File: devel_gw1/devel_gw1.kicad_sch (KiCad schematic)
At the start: 179 parts, among them Q1 2N7002, Q10 2N7002, Q11 2N7002, Q12 2N7002, Q13 2N7002, Q14 2N7002, Q15 2N7002, Q16 2N7002, Q17 2N7002, Q18 2N7002, Q19 2N7002, Q2 2N7002, Q20 2N7002, Q21 2N7002, Q22 2N7002, Q23 2N7002, Q24 2N7002, Q25 2N7002, Q26 2N7002, Q27 2N7002, Q28 2N7002, Q29 2N7002, Q3 2N7002, Q30 2N7002, Q31 2N7002, Q32 2N7002, Q33 2N7002, Q34 2N7002, Q35 2N7002, Q36 2N7002, Q37 2N7002, Q38 2N7002, Q39 2N7002, Q4 2N7002, Q41 2N7002, Q5 2N7002, Q6 2N7002, Q7 2N7002, Q8 2N7002, Q9 2N7002, U1 GW1N-LV9QN88C6_I5_, U2 LM3480-3.3, U3 AP2202K-ADJ, U4 ESP-PSRAM32, U5 AT25SF081-XMHF-X, U6 AP62150Z6, X1 ASE-xxxMHz

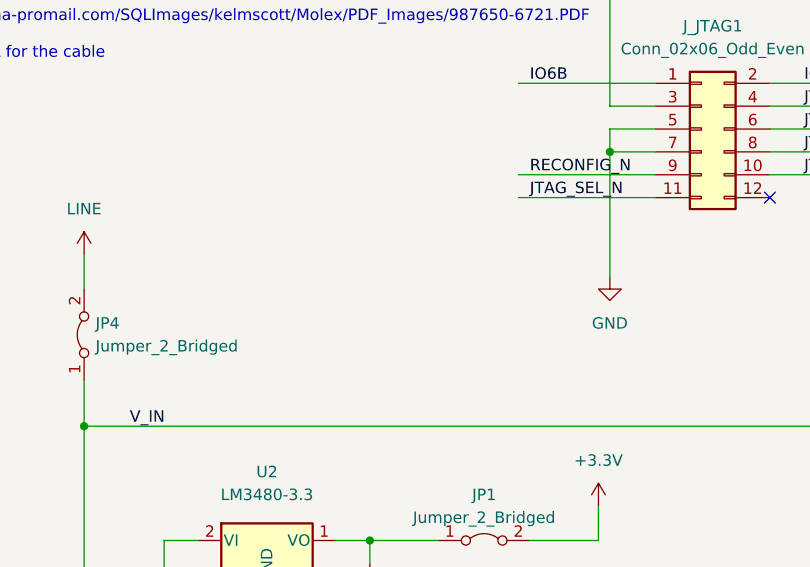
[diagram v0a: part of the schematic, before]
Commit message: Added power input connector
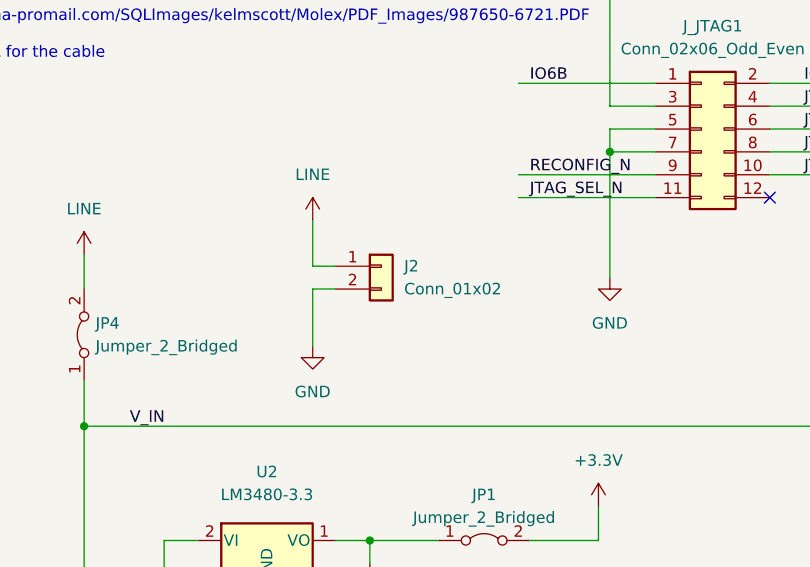
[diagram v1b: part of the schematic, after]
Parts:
- added J2: Conn_01x02, Connector_PinHeader_2.54mm:PinHeader_1x02_P2.54mm_Vertical, symbol Connector_Generic:Conn_01x02
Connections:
- net GND: now also J2.2 (Pin_2)
- net LINE: now also J2.1 (Pin_1)
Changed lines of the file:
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@@
     (stroke (width 0) (type default))
   )
+  (wire (pts (xy 157.48 220.98) (xy 157.48 226.06))
+    (stroke (width 0) (type default))
+  )
   (wire (pts (xy 228.6 71.12) (xy 228.6 73.66))
     (stroke (width 0) (type default))
@@
     (stroke (width 0) (type default))
   )
+  (wire (pts (xy 160.02 228.6) (xy 157.48 228.6))
+    (stroke (width 0) (type default))
+  )
   (wire (pts (xy 222.25 265.43) (xy 219.71 265.43))
     (stroke (width 0) (type default))
@@
     (stroke (width 0) (type default))
   )
+  (wire (pts (xy 160.02 226.06) (xy 157.48 226.06))
+    (stroke (width 0) (type default))
+  )
   (wire (pts (xy 107.95 154.94) (xy 133.35 154.94))
     (stroke (width 0) (type default))
@@
     (stroke (width 0) (type default))
   )
+  (wire (pts (xy 157.48 228.6) (xy 157.48 234.95))
+    (stroke (width 0) (type default))
+  )
   (wire (pts (xy 107.95 157.48) (xy 133.35 157.48))
     (stroke (width 0) (type default))
@@
     )
   )
+  (symbol (lib_id "Connector_Generic:Conn_01x02") (at 165.1 226.06 0) (unit 1)
+    (in_bom yes) (on_board yes) (dnp no) (fields_autoplaced)
+    (property "Reference" "J2" (at 167.64 226.06 0)
+      (effects (font (size 1.27 1.27)) (justify left))
+    )
+    (property "Value" "Conn_01x02" (at 167.64 228.6 0)
+      (effects (font (size 1.27 1.27)) (justify left))
+    )
+    (property "Footprint" "Connector_PinHeader_2.54mm:PinHeader_1x02_P2.54mm_Vertical" (at 165.1 226.06 0)
+      (effects (font (size 1.27 1.27)) hide)
+    )
+    (property "Datasheet" "~" (at 165.1 226.06 0)
+      (effects (font (size 1.27 1.27)) hide)
+    )
+    (pin "1")
+    (pin "2")
+    (instances
+      (project "devel_gw1"
+        (path "/f6df1e3b-3728-4bb2-8d84-c5251d58c11a"
+          (reference "J2") (unit 1)
+        )
+      )
+    )
+  )
   (symbol (lib_id "power:GND") (at 457.2 283.21 0) (unit 1)
     (in_bom yes) (on_board yes) (dnp no) (fields_autoplaced)
@@
     )
   )
+  (symbol (lib_id "power:GND") (at 157.48 234.95 0) (unit 1)
+    (in_bom yes) (on_board yes) (dnp no) (fields_autoplaced)
+    (property "Reference" "#PWR020" (at 157.48 241.3 0)
+      (effects (font (size 1.27 1.27)) hide)
+    )
+    (property "Value" "GND" (at 157.48 240.03 0)
+      (effects (font (size 1.27 1.27)))
+    )
+    (property "Footprint" "" (at 157.48 234.95 0)
+      (effects (font (size 1.27 1.27)) hide)
+    )
+    (property "Datasheet" "" (at 157.48 234.95 0)
+      (effects (font (size 1.27 1.27)) hide)
+    )
+    (pin "1")
+    (instances
+      (project "devel_gw1"
+        (path "/f6df1e3b-3728-4bb2-8d84-c5251d58c11a"
+          (reference "#PWR020") (unit 1)
+        )
+      )
+    )
+  )
   (symbol (lib_id "power:+3.3V") (at 490.22 92.71 0) (unit 1)
     (in_bom yes) (on_board yes) (dnp no) (fields_autoplaced)
@@
         )
       )
+    )
+  )
+  (symbol (lib_id "power:LINE") (at 157.48 220.98 0) (unit 1)
+    (in_bom yes) (on_board yes) (dnp no)
+    (property "Reference" "#PWR019" (at 157.48 224.79 0)
+      (effects (font (size 1.27 1.27)) hide)
+    )
+    (property "Value" "LINE" (at 157.48 215.9 0)
+      (effects (font (size 1.27 1.27)))
+    )
+    (property "Footprint" "" (at 157.48 220.98 0)
+      (effects (font (size 1.27 1.27)) hide)
+    )
+    (property "Datasheet" "" (at 157.48 220.98 0)
+      (effects (font (size 1.27 1.27)) hide)
+    )
+    (pin "1")
+    (instances
+      (project "devel_gw1"
+        (path "/f6df1e3b-3728-4bb2-8d84-c5251d58c11a"
+          (reference "#PWR019") (unit 1)
+        )
+      )

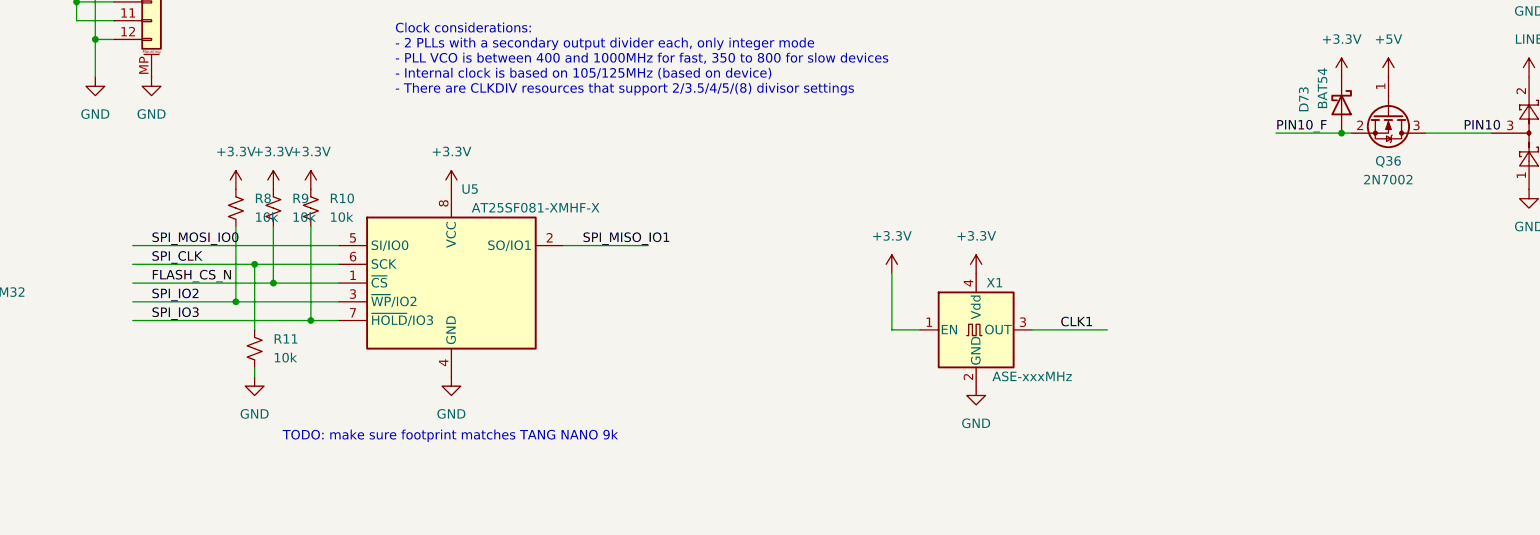
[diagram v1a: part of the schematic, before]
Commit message: Replaced TSSOP FLASH with SO-8 one due to availability concerns.
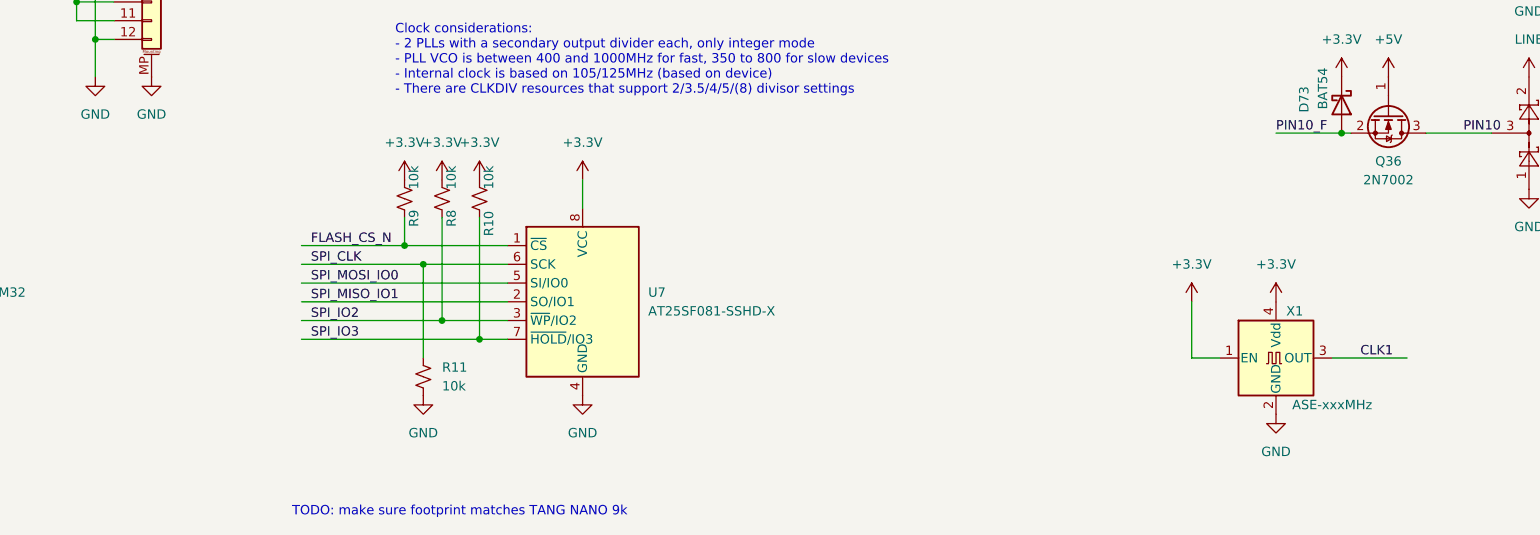
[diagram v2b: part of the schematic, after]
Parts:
- removed U5: AT25SF081-XMHF-X, Package_SO:TSSOP-8_4.4x3mm_P0.65mm, symbol Memory_Flash:AT25SF081-XMHF-X
- added U7: AT25SF081-SSHD-X, Package_SO:SOIC-8_3.9x4.9mm_P1.27mm, symbol Memory_Flash:AT25SF081-SSHD-X
- D1, D11, D13, D15, D17, D19, D2, D21, D23, D25, D27, D29, D31, D33, D35, D37, D39, D4, D41, D43, D45, D47, D49, D51, D53, D55, D57, D59, D6, D61, D63, D65, D67, D69, D71, D73, D75, D77, D79, D8: MP (none) -> BAT54-7-F
- D10, D12, D14, D16, D18, D20, D22, D24, D26, D28, D3, D30, D32, D34, D36, D38, D40, D42, D44, D46, D48, D5, D50, D52, D54, D56, D58, D60, D62, D64, D66, D68, D7, D70, D72, D74, D76, D78, D80, D9: MP (none) -> BAT54S-7-F
- Q1, Q10, Q11, Q12, Q13, Q14, Q15, Q16, Q17, Q18, Q19, Q2, Q20, Q21, Q22, Q23, Q24, Q25, Q26, Q27, Q28, Q29, Q3, Q30, Q31, Q32, Q33, Q34, Q35, Q36, Q37, Q38, Q39, Q4, Q41, Q5, Q6, Q7, Q8, Q9: MP (none) -> NDS7002A
- U2: MP (none) -> LM3480IM3X-3.3/NOPB
- U3: MP (none) -> AP2202K-ADJTRE1
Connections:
- net +3V3: now also U7.8 (VCC)
- net FLASH_CS_N: now also U7.1 (~{CS})
- net GND: now also U7.4 (GND)
- net SPI_CLK: now also U7.6 (SCK)
- net SPI_IO2: now also U7.3 (~{WP}/IO2)
- net SPI_IO3: now also U7.7 (~{HOLD}/IO3)
- net SPI_MISO_IO1: now also U7.2 (SO/IO1)
- net SPI_MOSI_IO0: now also U7.5 (SI/IO0)
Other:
- moved on the sheet: R10, R11, R8, R9, X1

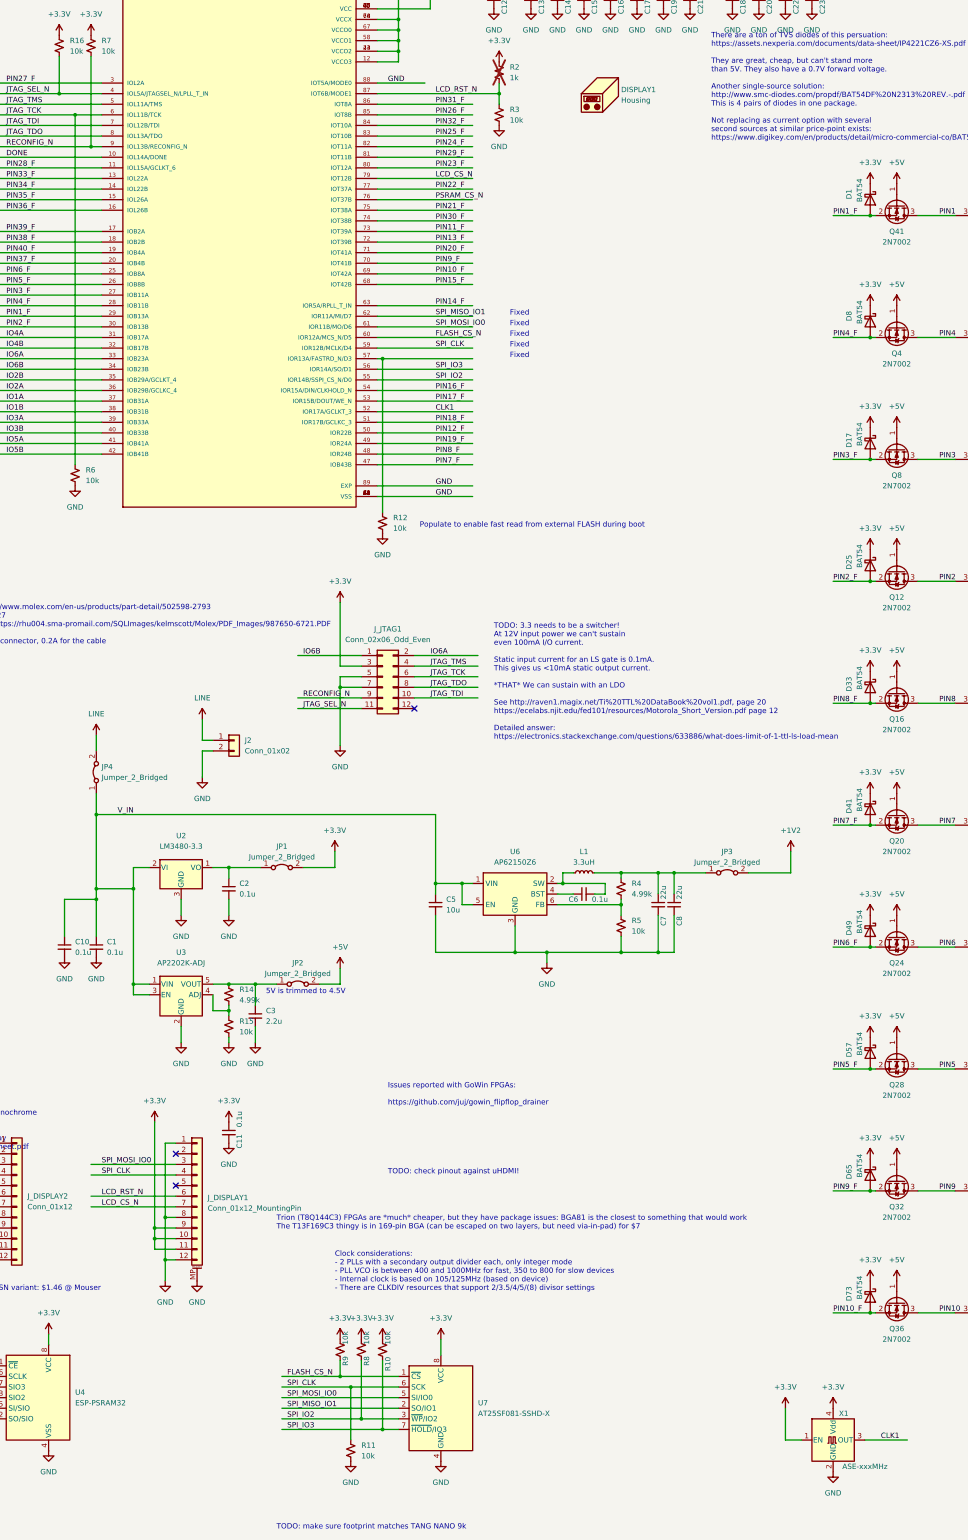
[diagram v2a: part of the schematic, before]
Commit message: Populated part numbers for most parts.
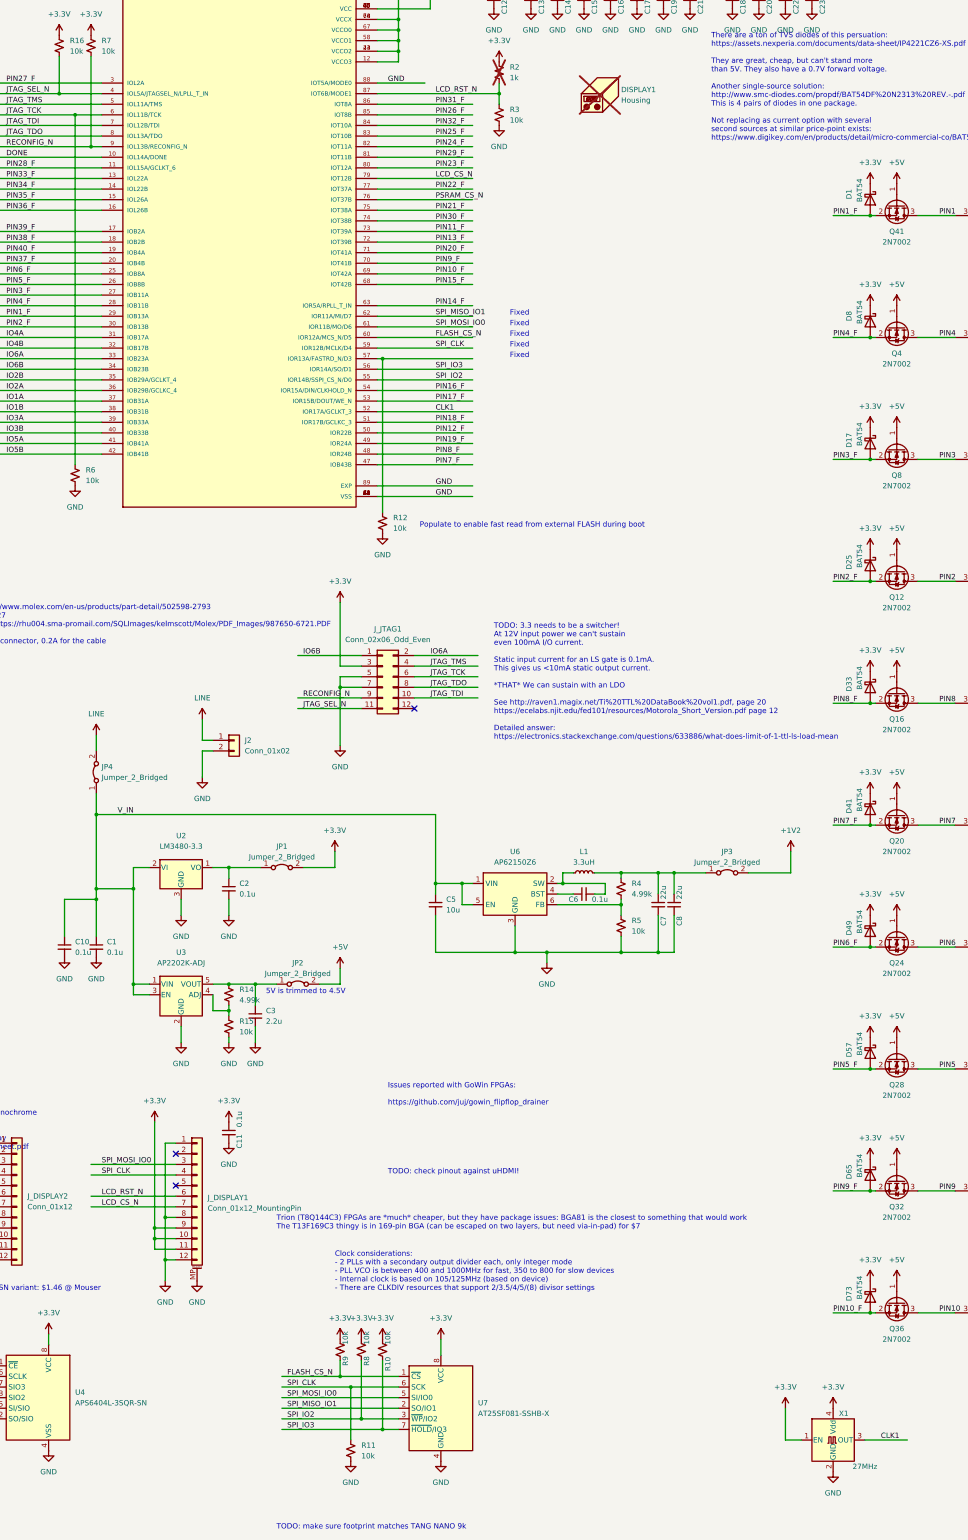
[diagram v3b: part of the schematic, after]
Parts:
- DISPLAY1: now not fitted
- J2, JP1, JP2, JP3, JP4: MP (none) -> PRPC002SAAN-RC
- J_DISPLAY1: footprint UNIC:CF31121D0R0-05-NH -> UNIC:HRS_FH19C-12S-0.5SH_05_; MP (none) -> FH19C-12S-0.5SH(10)
- J_DISPLAY2: MP (none) -> PRPC012SAAN-RC
- J_EXT1: MP (none) -> 502598-2793
- J_EXT2: MP (none) -> PRPC014DAAN-RC
- J_JTAG1: MP (none) -> 10152265-1121HF
- L1: MP (none) -> WIP252012S-3R3MLDG
- LED_DONE1: MP (none) -> CS42C-QL4
- U4: value ESP-PSRAM32 -> APS6404L-3SQR-SN; MP (none) -> APS6404L-3SQR-SN
- U6: MP (none) -> AP62150Z6-7
- U7: value AT25SF081-SSHD-X -> AT25SF081-SSHB-X; MP (none) -> AT25SF081B-SSHB-T
- X1: value ASE-xxxMHz -> 27MHz; MP (none) -> O 27\,0-JO32-B-1V3-1-T1-LF
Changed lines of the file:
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@@
       (effects (font (size 1.27 1.27)) hide)
     )
+    (property "MP" "PRPC014DAAN-RC" (at 43.18 171.45 0)
+      (effects (font (size 1.27 1.27)) hide)
+    )
     (pin "20")
     (pin "15")
@@
       (effects (font (size 1.27 1.27)) hide)
     )
+    (property "MP" "AP62150Z6-7" (at 232.41 262.89 0)
+      (effects (font (size 1.27 1.27)) hide)
+    )
     (pin "1")
     (pin "2")
@@
       (effects (font (size 1.27 1.27)) hide)
     )
+    (property "MP" "PRPC002SAAN-RC" (at 165.1 226.06 0)
+      (effects (font (size 1.27 1.27)) hide)
+    )
     (pin "1")
     (pin "2")
@@
       (effects (font (size 1.27 1.27)) (justify left))
     )
-    (property "Footprint" "UNIC:CF31121D0R0-05-NH" (at 156.21 335.28 0)
+    (property "Footprint" "UNIC:HRS_FH19C-12S-0.5SH_05_" (at 156.21 335.28 0)
       (effects (font (size 1.27 1.27)) hide)
     )
@@
       (effects (font (size 1.27 1.27)) hide)
     )
+    (property "MP" "FH19C-12S-0.5SH(10)" (at 156.21 335.28 0)
+      (effects (font (size 1.27 1.27)) hide)
+    )
     (pin "1")
     (pin "10")
@@
       (effects (font (size 1.27 1.27)) hide)
     )
-    (property "Datasheet" "~" (at 248.92 257.81 0)
+    (property "Datasheet" "https://mm.digikey.com/Volume0/opasdata/d220001/medias/docus/5561/WIP252012S%20L%20Series.pdf" (at 248.92 257.81 0)
+      (effects (font (size 1.27 1.27)) hide)
+    )
+    (property "MP" "WIP252012S-3R3MLDG" (at 248.92 257.81 90)
       (effects (font (size 1.27 1.27)) hide)
     )
@@
       (effects (font (size 1.27 1.27)) hide)
     )
+    (property "MP" "PRPC002SAAN-RC" (at 180.34 284.48 0)
+      (effects (font (size 1.27 1.27)) hide)
+    )
     (pin "1")
     (pin "2")
@@
       (effects (font (size 1.27 1.27)) hide)
     )
+    (property "MP" "PRPC012SAAN-RC" (at 113.03 335.28 0)
+      (effects (font (size 1.27 1.27)) hide)
+    )
     (pin "7")
     (pin "3")
@@
       (effects (font (size 1.27 1.27)) hide)
     )
+    (property "MP" "502598-2793" (at 82.55 171.45 0)
+      (effects (font (size 1.27 1.27)) hide)
+    )
     (pin "1")
     (pin "10")
@@
       (effects (font (size 1.27 1.27)) hide)
     )
+    (property "MP" "PRPC002SAAN-RC" (at 176.53 256.54 0)
+      (effects (font (size 1.27 1.27)) hide)
+    )
     (pin "2")
     (pin "1")
@@
   )
   (symbol (lib_id "Mechanical:Housing") (at 254 71.12 0) (unit 1)
-    (in_bom yes) (on_board yes) (dnp no) (fields_autoplaced)
+    (in_bom yes) (on_board yes) (dnp yes) (fields_autoplaced)
     (property "Reference" "DISPLAY1" (at 257.81 70.1674 0)
       (effects (font (size 1.27 1.27)) (justify left))
@@
       (effects (font (size 1.27 1.27)) (justify right))
     )
-    (property "Value" "ESP-PSRAM32" (at 127 384.8099 0)
+    (property "Value" "APS6404L-3SQR-SN" (at 127 384.8099 0)
       (effects (font (size 1.27 1.27)) (justify right))
     )
@@
       (effects (font (size 1.27 1.27)) hide)
     )
-    (property "Datasheet" "https://www.espressif.com/sites/default/files/documentation/esp-psram32_datasheet_en.pdf" (at 128.27 370.84 0)
+    (property "Datasheet" "https://www.mouser.com/datasheet/2/1127/APM_PSRAM_QSPI_APS6404L_3SQR_v2_3_PKG-1954826.pdf" (at 128.27 370.84 0)
+      (effects (font (size 1.27 1.27)) hide)
+    )
+    (property "MP" "APS6404L-3SQR-SN" (at 118.11 383.54 0)
       (effects (font (size 1.27 1.27)) hide)
     )
@@
       (effects (font (size 1.27 1.27)))
     )
-    (property "Value" "ASE-xxxMHz" (at 316.23 400.05 0)
+    (property "Value" "27MHz" (at 316.23 400.05 0)
       (effects (font (size 1.27 1.27)))
     )
@@
       (effects (font (size 1.27 1.27)) hide)
     )
-    (property "Datasheet" "http://www.abracon.com/Oscillators/ASV.pdf" (at 306.07 393.7 0)
+    (property "Datasheet" "https://www.jauch.com/downloadfile/5ef1edcfb8e2f73163c8ce8009ef659d1/jo32-1.8-3.3v.pdf" (at 306.07 393.7 0)
+      (effects (font (size 1.27 1.27)) hide)
+    )
+    (property "MP" "O 27\\,0-JO32-B-1V3-1-T1-LF" (at 308.61 393.7 0)
       (effects (font (size 1.27 1.27)) hide)
     )
@@
       (effects (font (size 1.27 1.27)) (justify left))
     )
-    (property "Value" "AT25SF081-SSHD-X" (at 223.52 387.35 0)
+    (property "Value" "AT25SF081-SSHB-X" (at 223.52 387.35 0)
       (effects (font (size 1.27 1.27)) (justify left))
     )
@@
       (effects (font (size 1.27 1.27)) hide)
     )
-    (property "Datasheet" "https://www.adestotech.com/wp-content/uploads/DS-AT25SF081_045.pdf" (at 214.63 386.08 0)
+    (property "Datasheet" "https://www.renesas.com/us/en/document/dst/at25sf081b-datasheet" (at 214.63 386.08 0)
+      (effects (font (size 1.27 1.27)) hide)
+    )
+    (property "MP" "AT25SF081B-SSHB-T" (at 214.63 386.08 0)
       (effects (font (size 1.27 1.27)) hide)
     )
@@
       (effects (font (size 1.27 1.27)) hide)
     )
+    (property "MP" "PRPC002SAAN-RC" (at 132.08 233.68 0)
+      (effects (font (size 1.27 1.27)) hide)
+    )
     (pin "2")
     (pin "1")
@@
       (effects (font (size 1.27 1.27)) hide)
     )
-    (property "Datasheet" "~" (at 67.31 100.33 0)
+    (property "Datasheet" "https://chromeled.com/pdf/smd/CS42C-QL4.pdf" (at 67.31 100.33 0)
+      (effects (font (size 1.27 1.27)) hide)
+    )
+    (property "MP" "CS42C-QL4" (at 67.31 100.33 90)
       (effects (font (size 1.27 1.27)) hide)
     )
@@
       (effects (font (size 1.27 1.27)) hide)
     )
+    (property "MP" "PRPC002SAAN-RC" (at 283.21 257.81 0)
+      (effects (font (size 1.27 1.27)) hide)
+    )
     (pin "2")
     (pin "1")
@@
       (effects (font (size 1.27 1.27)) hide)
     )
+    (property "MP" "10152265-1121HF" (at 200.66 210.82 0)
+      (effects (font (size 1.27 1.27)) hide)
+    )
